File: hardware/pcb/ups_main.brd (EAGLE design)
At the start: 121.9 x 59.7 mm, 83 parts, among them IC1 LTC4416EMS-1#PBF, IC2 LTC4079EDD#TRPBF, IC3 STM32F405RGT6, IC4 TPS613782QWRTERQ1, IC5 MCS1802GS-20-Z, J1 694106301002, J2 694106301002, J3 694106301002, Q1 IPD068P03L3GATMA1, Q2 IPD068P03L3GATMA1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

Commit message: update schem
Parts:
- R12: value 158k -> 280k
- R13: value 158k -> 20k
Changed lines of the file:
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@@
 <attribute name="VALUE" x="-13.462" y="84.582" size="1.27" layer="27" rot="R90"/>
 </element>
-<element name="R12" library="rcl" library_urn="urn:adsk.eagle:library:334" package="R0603" package3d_urn="urn:adsk.eagle:package:23555/3" value="158k" x="24.765" y="85.344" smashed="yes" rot="R90">
+<element name="R12" library="rcl" library_urn="urn:adsk.eagle:library:334" package="R0603" package3d_urn="urn:adsk.eagle:package:23555/3" value="280k" x="24.765" y="85.344" smashed="yes" rot="R90">
 <attribute name="NAME" x="21.336" y="89.408" size="0.8128" layer="25" rot="R270"/>
 <attribute name="POPULARITY" value="70" x="24.765" y="85.344" size="1.778" layer="27" rot="R90" display="off"/>
@@
 <attribute name="VALUE" x="26.67" y="84.709" size="1.27" layer="27" rot="R90"/>
 </element>
-<element name="R13" library="rcl" library_urn="urn:adsk.eagle:library:334" package="R0603" package3d_urn="urn:adsk.eagle:package:23555/3" value="158k" x="27.305" y="84.074" smashed="yes" rot="R180">
+<element name="R13" library="rcl" library_urn="urn:adsk.eagle:library:334" package="R0603" package3d_urn="urn:adsk.eagle:package:23555/3" value="20k" x="27.305" y="84.074" smashed="yes" rot="R180">
 <attribute name="NAME" x="31.242" y="84.455" size="0.8128" layer="25" rot="R180"/>
 <attribute name="POPULARITY" value="70" x="27.305" y="84.074" size="1.778" layer="27" rot="R180" display="off"/>

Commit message: fix errors in schem/layout
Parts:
- added C24: T491D226M035AT, T491D226M035AT:T491D
- added C25: 1uF, rcl:C0603K
- added C26: 22uF, rcl:C0603K
- moved C9 0.13 mm to (27.4, 80.8)
- moved R13 0.13 mm to (27.4, 84.1)
- moved R16 0.13 mm to (27.4, 82.4)
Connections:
- removed net N$29: C10.2, IC4.6
- new net N$37: C10.2, IC4.15, IC4.6
- net +12V: now also C24.1
- net GND: now also C24.2, C25.1, C26.1
- net VBAT1: now also C25.2
- net VBAT2: now also C26.2; no longer IC4.15
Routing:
- net N$37: track 0.00 -> 14.6 mm, vias 0 -> 2
- net VBAT2: track 19.4 -> 14.6 mm
- net N$29: track 1.59 -> 0.00 mm
- net GND: track 209.9 -> 210.5 mm

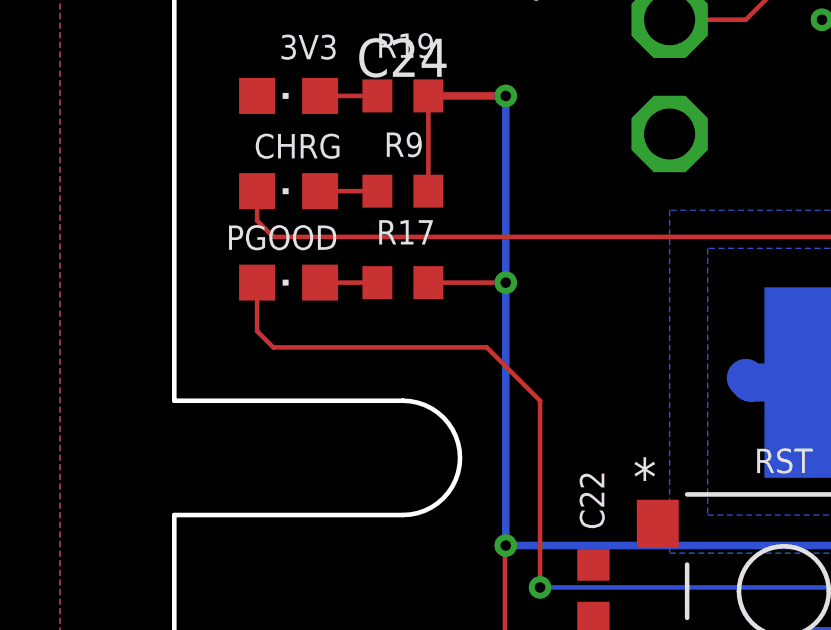
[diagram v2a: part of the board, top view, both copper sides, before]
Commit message: fix pgood led
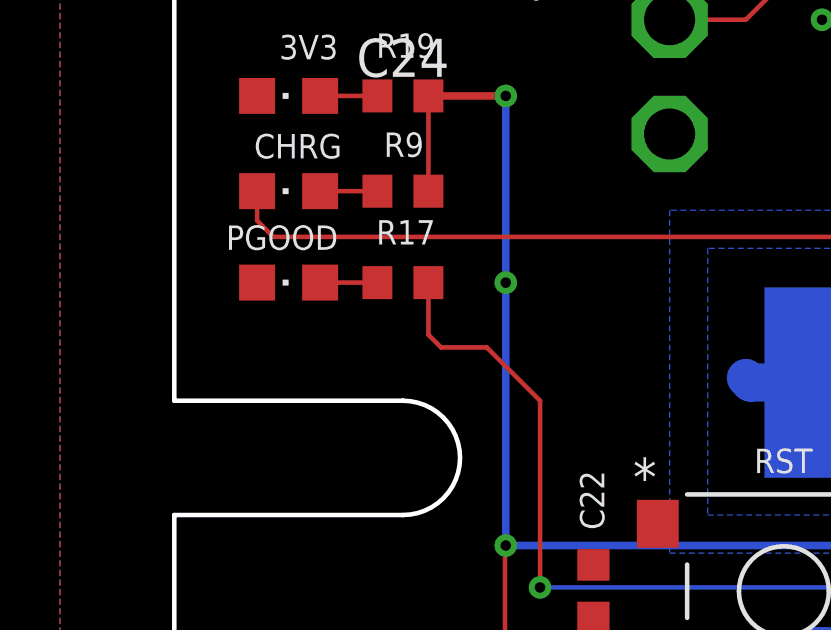
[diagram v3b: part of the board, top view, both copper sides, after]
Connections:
- net +3V3: no longer R17.2
- net GND: now also PGOOD.C
- net N$13: now also R17.2; no longer PGOOD.C
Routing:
- net N$13: track 81.9 -> 76.2 mm
- net +3V3: track 275.0 -> 272.4 mm
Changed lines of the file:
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@@
 <contactref element="C25" pad="1"/>
 <contactref element="C26" pad="1"/>
+<contactref element="PGOOD" pad="C"/>
 <wire x1="-15.367" y1="86.067" x2="-12.319" y2="86.868" width="0" layer="19" extent="1-16"/>
 </signal>
@@
 <contactref element="R9" pad="2"/>
 <wire x1="-27.09" y1="70.485" x2="-27.09" y2="73.66" width="0.1524" layer="1"/>
-<contactref element="R17" pad="2"/>
-<wire x1="-27.09" y1="67.437" x2="-24.511" y2="67.437" width="0.1524" layer="1"/>
 <via x="-24.511" y="67.437" extent="1-16" drill="0.35"/>
 <wire x1="-24.511" y1="67.437" x2="-24.511" y2="67.31" width="0.1524" layer="16"/>
@@
 <wire x1="25.4" y1="75.946" x2="25.4" y2="81.788" width="0.1524" layer="16"/>
 <wire x1="6.731" y1="57.277" x2="-23.368" y2="57.277" width="0.1524" layer="16"/>
-<contactref element="PGOOD" pad="C"/>
-<wire x1="-32.8" y1="67.437" x2="-32.8" y2="65.82" width="0.1524" layer="1"/>
-<wire x1="-32.8" y1="65.82" x2="-32.258" y2="65.278" width="0.1524" layer="1"/>
 <wire x1="-25.146" y1="65.278" x2="-23.368" y2="63.5" width="0.1524" layer="1"/>
-<wire x1="-32.258" y1="65.278" x2="-25.146" y2="65.278" width="0.1524" layer="1"/>
+<contactref element="R17" pad="2"/>
+<wire x1="-26.67" y1="65.278" x2="-25.146" y2="65.278" width="0.1524" layer="1"/>
+<wire x1="-26.67" y1="65.278" x2="-27.09" y2="65.698" width="0.1524" layer="1"/>
+<wire x1="-27.09" y1="65.698" x2="-27.09" y2="67.437" width="0.1524" layer="1"/>
 </signal>
 <signal name="N$21">
